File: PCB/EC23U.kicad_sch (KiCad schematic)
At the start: 28 parts, among them J1 JST, J2 RGB, SW1 BOOT0, U1 STM32F401CBUx, U2 XC6206PxxxMR, U5 SN74AHCT1G125, Y1 8 MHz

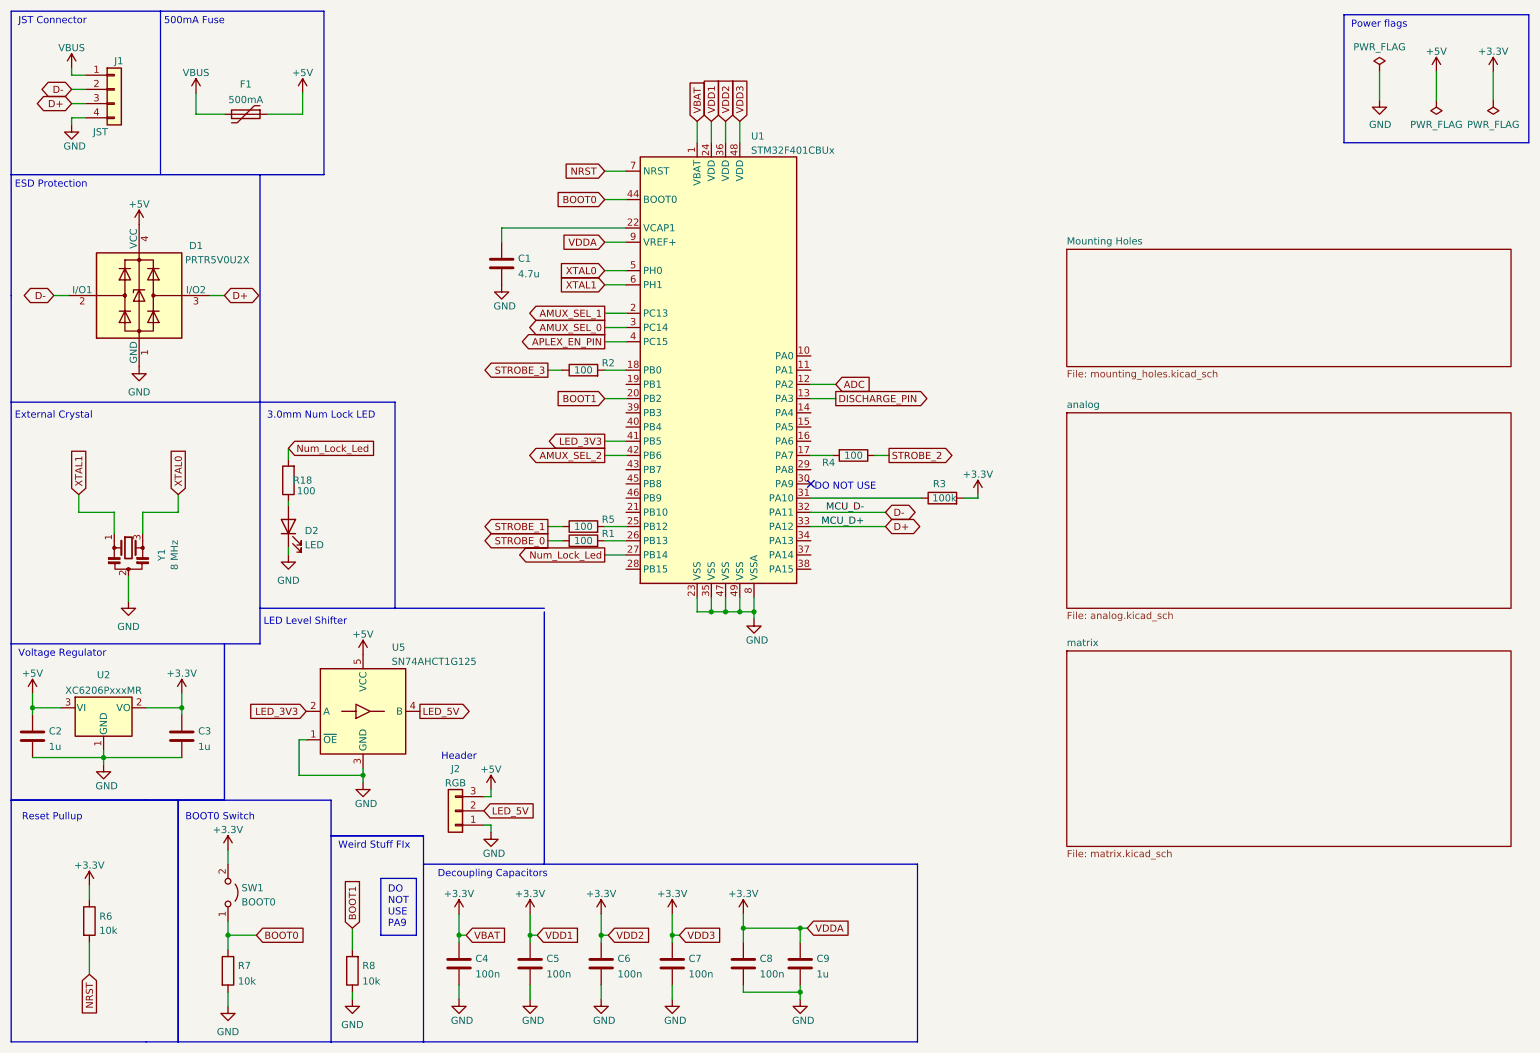
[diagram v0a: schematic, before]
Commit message: Update
Updated the License for the project and relative details.
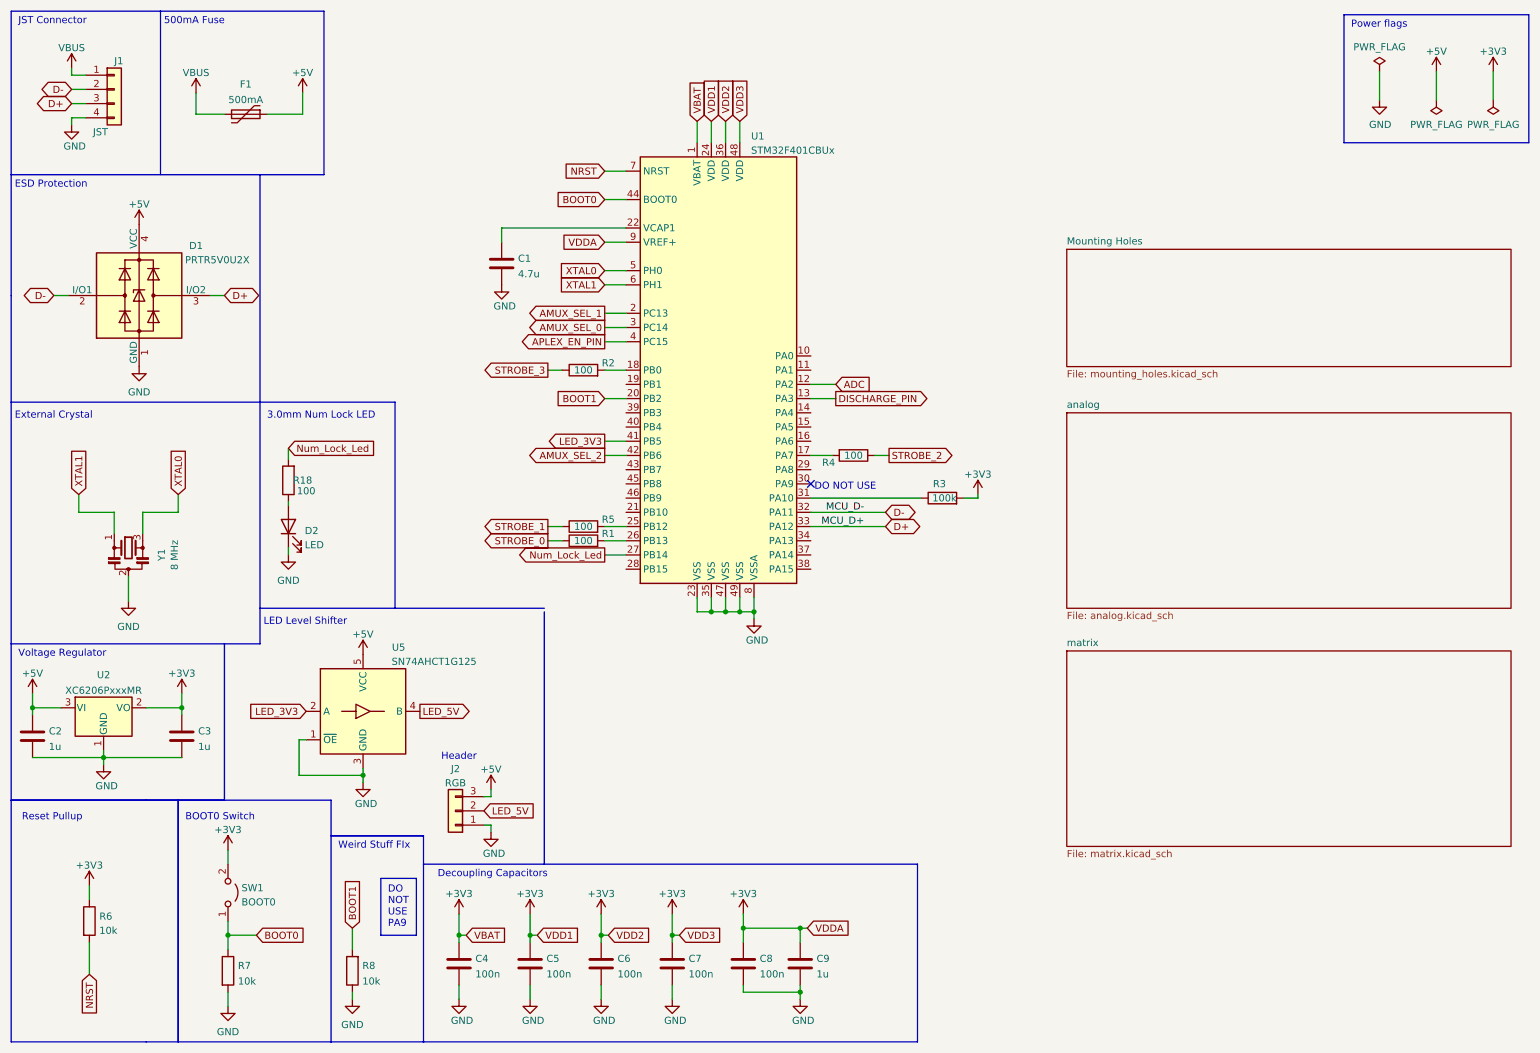
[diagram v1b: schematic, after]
